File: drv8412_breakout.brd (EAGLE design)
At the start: 64.4 x 39.4 mm, 1 part

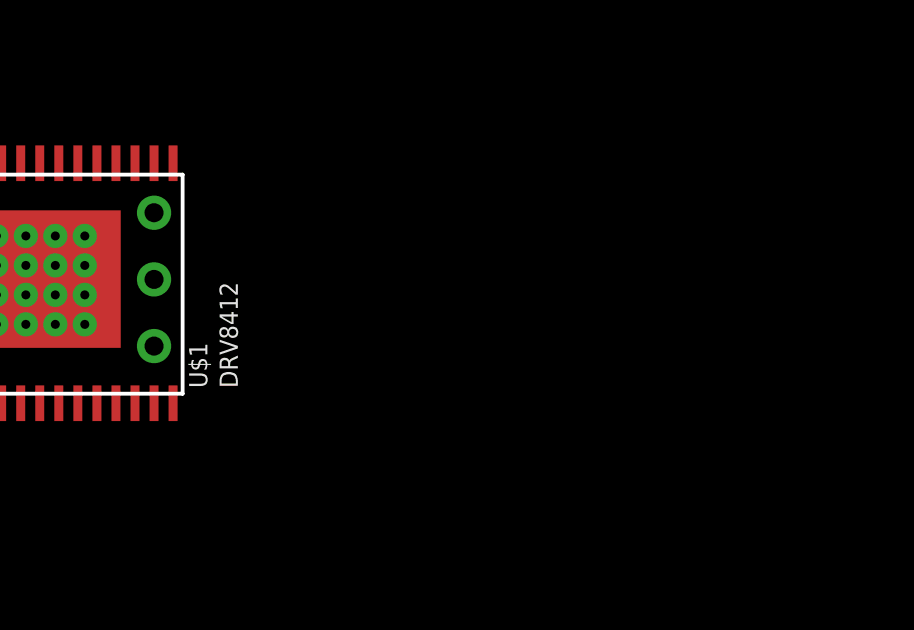
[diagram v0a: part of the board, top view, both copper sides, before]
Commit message: Added schematic and board layout
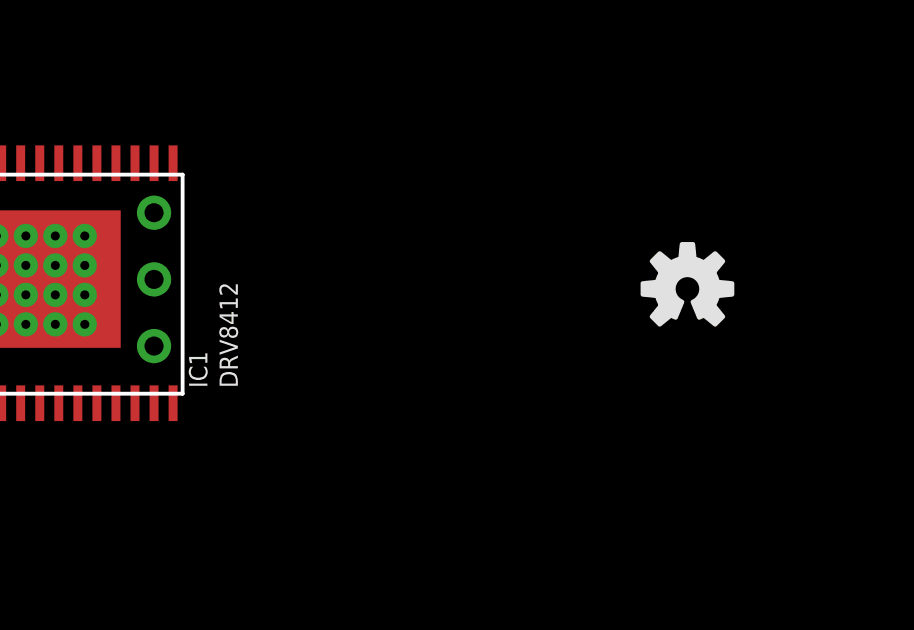
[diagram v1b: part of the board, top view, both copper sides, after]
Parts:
- added IC1: DRV8412TSSOP44, DRV8412:TSSOP24
- U$1: value DRV8412TSSOP44 -> (none); device DRV8412:TSSOP24 -> SparkFun-Aesthetics:OSHW-LOGO-S
- moved U$1 24.1 mm to (55.9, 20.3), turned to 0 degrees
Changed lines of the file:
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@@
 <layer number="48" name="Document" color="7" fill="1" visible="yes" active="yes"/>
 <layer number="49" name="Reference" color="7" fill="1" visible="yes" active="yes"/>
+<layer number="50" name="dxf" color="7" fill="1" visible="no" active="no"/>
 <layer number="51" name="tDocu" color="7" fill="1" visible="yes" active="yes"/>
 <layer number="52" name="bDocu" color="7" fill="1" visible="yes" active="yes"/>
+<layer number="53" name="tGND_GNDA" color="7" fill="9" visible="no" active="no"/>
+<layer number="54" name="bGND_GNDA" color="1" fill="9" visible="no" active="no"/>
+<layer number="56" name="wert" color="7" fill="1" visible="no" active="no"/>
 <layer number="90" name="Modules" color="5" fill="1" visible="no" active="no"/>
 <layer number="91" name="Nets" color="2" fill="1" visible="no" active="no"/>
@@
 <layer number="97" name="Info" color="7" fill="1" visible="no" active="no"/>
 <layer number="98" name="Guide" color="6" fill="1" visible="no" active="no"/>
+<layer number="100" name="Muster" color="7" fill="1" visible="no" active="no"/>
+<layer number="101" name="Patch_Top" color="12" fill="4" visible="yes" active="yes"/>
+<layer number="102" name="Vscore" color="7" fill="1" visible="yes" active="yes"/>
+<layer number="103" name="tMap" color="7" fill="1" visible="yes" active="yes"/>
+<layer number="104" name="Name" color="16" fill="1" visible="yes" active="yes"/>
+<layer number="105" name="tPlate" color="7" fill="1" visible="yes" active="yes"/>
+<layer number="106" name="bPlate" color="7" fill="1" visible="yes" active="yes"/>
+<layer number="107" name="Crop" color="7" fill="1" visible="yes" active="yes"/>
+<layer number="108" name="tplace-old" color="10" fill="1" visible="no" active="yes"/>
+<layer number="109" name="ref-old" color="11" fill="1" visible="no" active="yes"/>
+<layer number="116" name="Patch_BOT" color="9" fill="4" visible="yes" active="yes"/>
+<layer number="121" name="_tsilk" color="7" fill="1" visible="yes" active="yes"/>
+<layer number="122" name="_bsilk" color="7" fill="1" visible="yes" active="yes"/>
+<layer number="125" name="_tNames" color="7" fill="1" visible="yes" active="yes"/>
+<layer number="144" name="Drill_legend" color="7" fill="1" visible="yes" active="yes"/>
+<layer number="151" name="HeatSink" color="7" fill="1" visible="yes" active="yes"/>
+<layer number="199" name="Contour" color="7" fill="1" visible="yes" active="yes"/>
+<layer number="200" name="200bmp" color="1" fill="10" visible="yes" active="yes"/>
+<layer number="201" name="201bmp" color="2" fill="10" visible="yes" active="yes"/>
+<layer number="202" name="202bmp" color="3" fill="10" visible="yes" active="yes"/>
+<layer number="203" name="203bmp" color="4" fill="10" visible="yes" active="yes"/>
+<layer number="204" name="204bmp" color="5" fill="10" visible="yes" active="yes"/>
+<layer number="205" name="205bmp" color="6" fill="10" visible="yes" active="yes"/>
+<layer number="206" name="206bmp" color="7" fill="10" visible="yes" active="yes"/>
+<layer number="207" name="207bmp" color="8" fill="10" visible="yes" active="yes"/>
+<layer number="208" name="208bmp" color="9" fill="10" visible="yes" active="yes"/>
+<layer number="209" name="209bmp" color="7" fill="1" visible="yes" active="yes"/>
+<layer number="210" name="210bmp" color="7" fill="1" visible="yes" active="yes"/>
+<layer number="211" name="211bmp" color="7" fill="1" visible="yes" active="yes"/>
+<layer number="212" name="212bmp" color="7" fill="1" visible="yes" active="yes"/>
+<layer number="213" name="213bmp" color="7" fill="1" visible="yes" active="yes"/>
+<layer number="214" name="214bmp" color="7" fill="1" visible="yes" active="yes"/>
+<layer number="215" name="215bmp" color="7" fill="1" visible="yes" active="yes"/>
+<layer number="216" name="216bmp" color="7" fill="1" visible="yes" active="yes"/>
+<layer number="217" name="217bmp" color="18" fill="1" visible="no" active="no"/>
+<layer number="218" name="218bmp" color="19" fill="1" visible="no" active="no"/>
+<layer number="219" name="219bmp" color="20" fill="1" visible="no" active="no"/>
+<layer number="220" name="220bmp" color="21" fill="1" visible="no" active="no"/>
+<layer number="221" name="221bmp" color="22" fill="1" visible="no" active="no"/>
+<layer number="222" name="222bmp" color="23" fill="1" visible="no" active="no"/>
+<layer number="223" name="223bmp" color="24" fill="1" visible="no" active="no"/>
+<layer number="224" name="224bmp" color="25" fill="1" visible="no" active="no"/>
+<layer number="250" name="Descript" color="3" fill="1" visible="no" active="no"/>
+<layer number="251" name="SMDround" color="12" fill="11" visible="no" active="no"/>
+<layer number="254" name="cooling" color="7" fill="1" visible="yes" active="yes"/>
 </layers>
 <board>
@@
 </autorouter>
 <elements>
-<element name="U$1" library="DRV8412" package="TSSOP24" value="DRV8412TSSOP44" x="31.75" y="20.32" rot="R90"/>
+<element name="IC1" library="DRV8412" package="TSSOP24" value="DRV8412TSSOP44" x="31.75" y="20.32" rot="R90"/>
+<element name="U$1" library="SparkFun-Aesthetics" package="OSHW-LOGO-S" value="" x="55.88" y="20.32"/>
 </elements>
 <signals>
